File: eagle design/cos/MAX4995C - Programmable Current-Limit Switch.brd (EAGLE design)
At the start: 22.9 x 17.8 mm, 5 parts, among them IC1 MAX4995CAUT+T, J1 61300311121, J2 61300311121

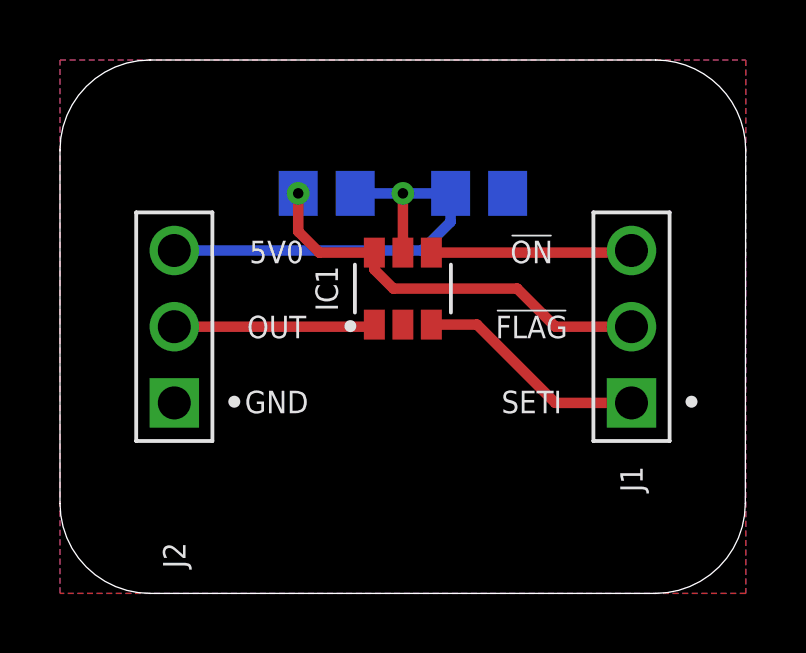
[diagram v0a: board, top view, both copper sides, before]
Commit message: HW rev.1 finished routing, created BOM, ERC & DRC check out fine, created gerbers
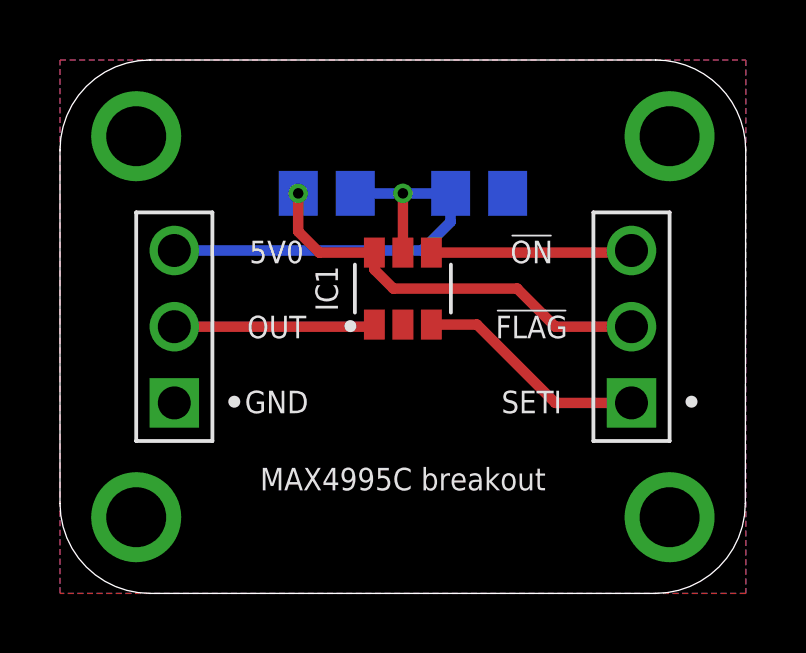
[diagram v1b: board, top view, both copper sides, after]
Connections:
- net VCC renamed 5V0
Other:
- board text added: "MAX4995C breakout"
- board text added: "ejovrh v.1"
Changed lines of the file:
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@@
 <setting verticaltext="up"/>
 </settings>
-<grid distance="0.25" unitdist="mm" unit="mm" style="lines" multiple="1" display="yes" altdistance="5" altunitdist="mil" altunit="mil"/>
+<grid distance="12.5" unitdist="mil" unit="mil" style="lines" multiple="1" display="yes" altdistance="5" altunitdist="mil" altunit="mil"/>
 <layers>
 <layer number="1" name="Top" color="4" fill="1" visible="yes" active="yes"/>
@@
 <text x="33.5" y="16.5" size="0.75" layer="21" font="vector" align="center">!FLAG!</text>
 <text x="33.5" y="14" size="0.75" layer="21" font="vector" align="center">SETI</text>
+<text x="29.21" y="11.43" size="0.75" layer="21" font="vector" align="center">MAX4995C breakout</text>
+<text x="29.21" y="12.7" size="0.75" layer="22" font="vector" rot="MR0" align="center">ejovrh v.1</text>
+<wire x1="37.465" y1="8.89" x2="20.955" y2="8.89" width="2.54" layer="29"/>
+<wire x1="20.955" y1="8.89" x2="19.05" y2="10.795" width="2.54" layer="29" curve="-90"/>
+<wire x1="19.05" y1="10.795" x2="19.05" y2="22.225" width="2.54" layer="29"/>
+<wire x1="19.05" y1="22.225" x2="20.955" y2="24.13" width="2.54" layer="29" curve="-90"/>
+<wire x1="20.955" y1="24.13" x2="37.465" y2="24.13" width="2.54" layer="29"/>
+<wire x1="37.465" y1="24.13" x2="39.37" y2="22.225" width="2.54" layer="29" curve="-90"/>
+<wire x1="39.37" y1="22.225" x2="39.37" y2="10.795" width="2.54" layer="29"/>
+<wire x1="39.37" y1="10.795" x2="37.465" y2="8.89" width="2.54" layer="29" curve="-90"/>
+<wire x1="19.05" y1="10.795" x2="19.05" y2="22.225" width="2.54" layer="30"/>
+<wire x1="19.05" y1="22.225" x2="20.955" y2="24.13" width="2.54" layer="30" curve="-90"/>
+<wire x1="20.955" y1="24.13" x2="37.465" y2="24.13" width="2.54" layer="30"/>
+<wire x1="37.465" y1="24.13" x2="39.37" y2="22.225" width="2.54" layer="30" curve="-90"/>
+<wire x1="39.37" y1="22.225" x2="39.37" y2="10.795" width="2.54" layer="30"/>
+<wire x1="39.37" y1="10.795" x2="37.465" y2="8.89" width="2.54" layer="30" curve="-90"/>
+<wire x1="37.465" y1="8.89" x2="20.955" y2="8.89" width="2.54" layer="30"/>
+<wire x1="20.955" y1="8.89" x2="19.05" y2="10.795" width="2.54" layer="30" curve="-90"/>
 </plain>
 <attributes>
@@
 </class>
 </classes>
-<designrules name="default">
-<description language="de">&lt;b&gt;EAGLE Design Rules&lt;/b&gt;
-&lt;p&gt;
-Die Standard-Design-Rules sind so gewählt, dass sie für
-die meisten Anwendungen passen. Sollte ihre Platine
-besondere Anforderungen haben, treffen Sie die erforderlichen
-Einstellungen hier und speichern die Design Rules unter
-einem neuen Namen ab.</description>
-<description language="en">&lt;b&gt;EAGLE Design Rules&lt;/b&gt;
+<designrules name="markovac_2layer">
+<description language="hr">&lt;b&gt;EAGLE Design Rules&lt;/b&gt;
 &lt;p&gt;
 The default Design Rules have been set to cover
@@
 <param name="mtCopper" value="0.035mm 0.035mm 0.035mm 0.035mm 0.035mm 0.035mm 0.035mm 0.035mm 0.035mm 0.035mm 0.035mm 0.035mm 0.035mm 0.035mm 0.035mm 0.035mm"/>
 <param name="mtIsolate" value="1.5mm 0.15mm 0.2mm 0.15mm 0.2mm 0.15mm 0.2mm 0.15mm 0.2mm 0.15mm 0.2mm 0.15mm 0.2mm 0.15mm 0.2mm"/>
-<param name="mdWireWire" value="6mil"/>
-<param name="mdWirePad" value="6mil"/>
-<param name="mdWireVia" value="6mil"/>
-<param name="mdPadPad" value="6mil"/>
-<param name="mdPadVia" value="6mil"/>
-<param name="mdViaVia" value="6mil"/>
-<param name="mdSmdPad" value="6mil"/>
-<param name="mdSmdVia" value="6mil"/>
-<param name="mdSmdSmd" value="6mil"/>
-<param name="mdViaViaSameLayer" value="6mil"/>
+<param name="mdWireWire" value="0.2mm"/>
+<param name="mdWirePad" value="0.2mm"/>
+<param name="mdWireVia" value="0.2mm"/>
+<param name="mdPadPad" value="0.2mm"/>
+<param name="mdPadVia" value="0.2mm"/>
+<param name="mdViaVia" value="0.2mm"/>
+<param name="mdSmdPad" value="0.2mm"/>
+<param name="mdSmdVia" value="0.2mm"/>
+<param name="mdSmdSmd" value="0.2mm"/>
+<param name="mdViaViaSameLayer" value="8mil"/>
 <param name="mnLayersViaInSmd" value="2"/>
-<param name="mdCopperDimension" value="40mil"/>
-<param name="mdDrill" value="6mil"/>
+<param name="mdCopperDimension" value="0.5mm"/>
+<param name="mdDrill" value="8mil"/>
 <param name="mdSmdStop" value="0mil"/>
-<param name="msWidth" value="6mil"/>
+<param name="msWidth" value="0.2mm"/>
 <param name="msDrill" value="0.35mm"/>
-<param name="msMicroVia" value="9.99mm"/>
+<param name="msMicroVia" value="0.25mm"/>
 <param name="msBlindViaRatio" value="0.5"/>
 <param name="rvPadTop" value="0.25"/>
@@
 <param name="rvMicroViaOuter" value="0.25"/>
 <param name="rvMicroViaInner" value="0.25"/>
-<param name="rlMinPadTop" value="10mil"/>
+<param name="rlMinPadTop" value="0.15mm"/>
 <param name="rlMaxPadTop" value="20mil"/>
 <param name="rlMinPadInner" value="10mil"/>
 <param name="rlMaxPadInner" value="20mil"/>
-<param name="rlMinPadBottom" value="10mil"/>
+<param name="rlMinPadBottom" value="0.15mm"/>
 <param name="rlMaxPadBottom" value="20mil"/>
-<param name="rlMinViaOuter" value="8mil"/>
+<param name="rlMinViaOuter" value="0.15mm"/>
 <param name="rlMaxViaOuter" value="20mil"/>
-<param name="rlMinViaInner" value="8mil"/>
+<param name="rlMinViaInner" value="0.1mm"/>
 <param name="rlMaxViaInner" value="20mil"/>
 <param name="rlMinMicroViaOuter" value="4mil"/>
@@
 <param name="mlMinCreamFrame" value="0mil"/>
 <param name="mlMaxCreamFrame" value="0mil"/>
-<param name="mlViaStopLimit" value="0mil"/>
+<param name="mlViaStopLimit" value="0.34mm"/>
 <param name="srRoundness" value="0"/>
 <param name="srMinRoundness" value="0mil"/>
 <param name="srMaxRoundness" value="0mil"/>
 <param name="slThermalIsolate" value="10mil"/>
-<param name="slThermalsForVias" value="0"/>
+<param name="slThermalsForVias" value="1"/>
 <param name="dpMaxLengthDifference" value="10mm"/>
 <param name="dpGapFactor" value="2.5"/>
-<param name="checkAngle" value="0"/>
+<param name="checkAngle" value="1"/>
 <param name="checkFont" value="1"/>
 <param name="checkRestrict" value="1"/>
@@
 </element>
 <element name="R1" library="rcl" library_urn="urn:adsk.eagle:library:334" package="R0805" package3d_urn="urn:adsk.eagle:package:23553/2" value="10k" x="26.67" y="20.955" smashed="yes" rot="MR180">
-<attribute name="NAME" x="26.21" y="16.955" size="0.75" layer="26" font="vector" rot="MR180" align="center"/>
+<attribute name="NAME" x="26.67" y="19.3675" size="0.75" layer="26" font="vector" rot="MR180" align="center"/>
 <attribute name="POPULARITY" value="86" x="26.67" y="20.955" size="1.778" layer="28" rot="MR180" display="off"/>
 <attribute name="SPICEPREFIX" value="R" x="26.67" y="20.955" size="1.778" layer="28" rot="MR180" display="off"/>
@@
 </element>
 <element name="C1" library="rcl" library_urn="urn:adsk.eagle:library:334" package="C0805" package3d_urn="urn:adsk.eagle:package:23617/2" value="1u" x="31.75" y="20.955" smashed="yes" rot="MR180">
-<attribute name="NAME" x="31.29" y="18.955" size="0.75" layer="26" font="vector" rot="MR180" align="center"/>
+<attribute name="NAME" x="31.75" y="19.3675" size="0.75" layer="26" font="vector" rot="MR180" align="center"/>
 <attribute name="POPULARITY" value="88" x="31.75" y="20.955" size="1.778" layer="28" rot="MR180" display="off"/>
 <attribute name="SPICEPREFIX" value="C" x="31.75" y="20.955" size="1.778" layer="28" rot="MR180" display="off"/>
@@
 <attribute name="MANUFACTURER" value="Wurth Electronics Inc." x="36.83" y="16.51" size="1.778" layer="27" rot="R90" display="off"/>
 <attribute name="MPN" value="61300311121" x="36.83" y="16.51" size="1.778" layer="27" rot="R90" display="off"/>
-<attribute name="NAME" x="36.83" y="11.43" size="0.75" layer="25" font="vector" rot="R90" align="center"/>
 <attribute name="VALUE" x="39.37" y="21.59" size="1.27" layer="27" rot="R90"/>
 </element>
@@
 <attribute name="MANUFACTURER" value="Wurth Electronics Inc." x="21.59" y="16.51" size="1.778" layer="27" rot="R90" display="off"/>
 <attribute name="MPN" value="61300311121" x="21.59" y="16.51" size="1.778" layer="27" rot="R90" display="off"/>
-<attribute name="NAME" x="21.59" y="8.89" size="0.75" layer="25" font="vector" rot="R90" align="center"/>
 <attribute name="VALUE" x="24.13" y="21.59" size="1.27" layer="27" rot="R90"/>
 </element>
@@
 <contactref element="C1" pad="2"/>
 <contactref element="J2" pad="1"/>
-<polygon width="0.381" layer="1">
+<polygon width="0.2" layer="1" spacing="1">
 <vertex x="17.78" y="25.4"/>
 <vertex x="40.64" y="25.4"/>
@@
 <vertex x="17.78" y="7.62"/>
 </polygon>
-<polygon width="0.381" layer="16">
+<polygon width="0.2" layer="16">
 <vertex x="17.78" y="25.4"/>
 <vertex x="40.64" y="25.4"/>
@@
 <vertex x="17.78" y="7.62"/>
 </polygon>
+<via x="20.32" y="22.86" extent="1-16" drill="2"/>
+<via x="38.1" y="22.86" extent="1-16" drill="2"/>
+<via x="20.32" y="10.16" extent="1-16" drill="2"/>
+<via x="38.1" y="10.16" extent="1-16" drill="2"/>
 </signal>
 <signal name="OUT" class="1">
@@
 <wire x1="28.19" y1="16.51" x2="21.59" y2="16.51" width="0.35" layer="1"/>
 </signal>
-<signal name="VCC" class="1">
+<signal name="5V0" class="1">
 <contactref element="IC1" pad="5_IN"/>
 <contactref element="C1" pad="1"/>
